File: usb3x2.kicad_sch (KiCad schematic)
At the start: 102 parts

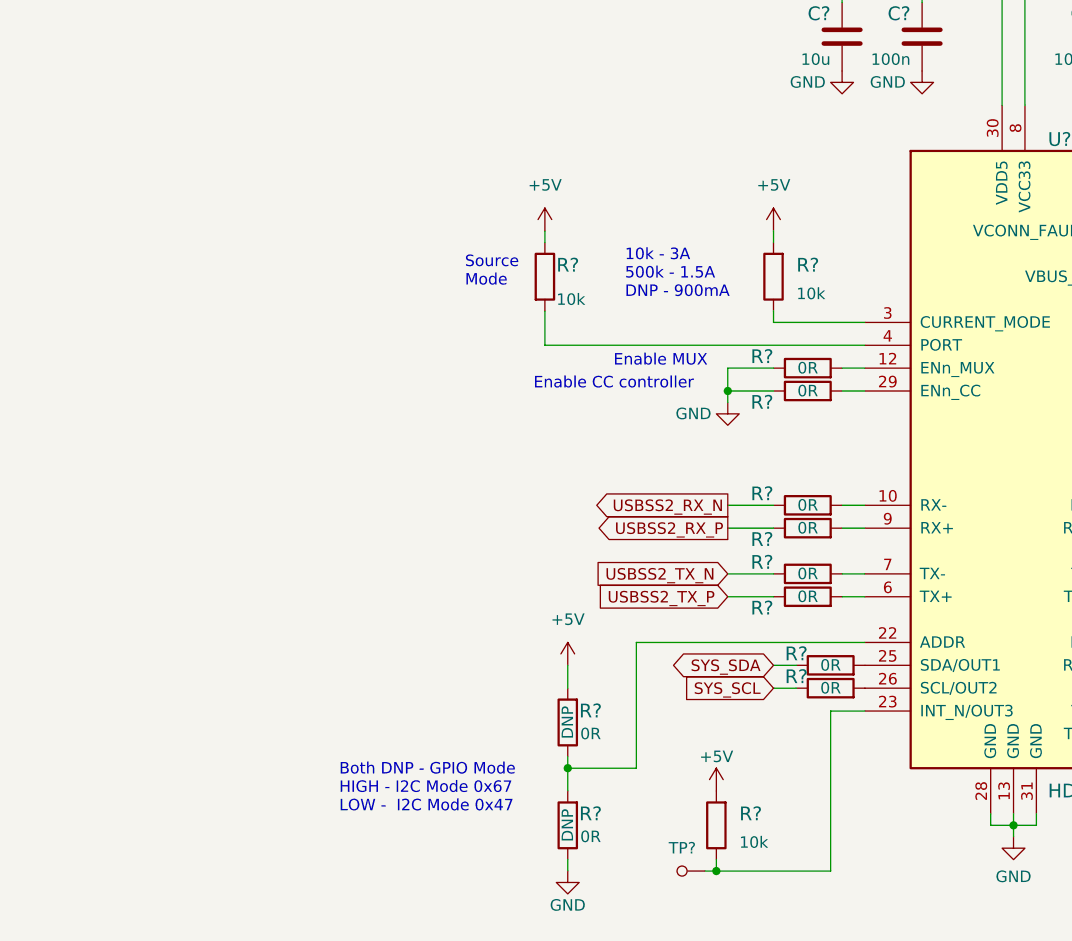
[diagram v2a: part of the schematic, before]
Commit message: Add labels to signals in usb3x2
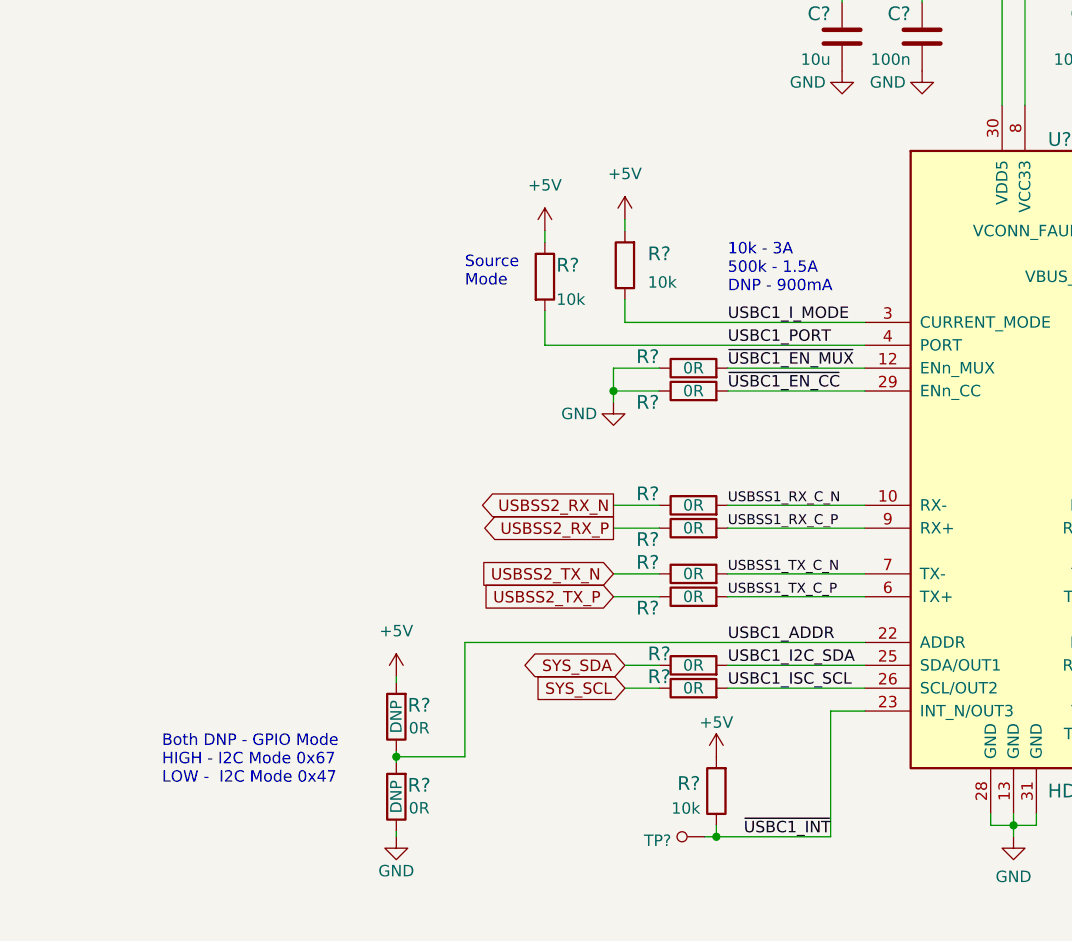
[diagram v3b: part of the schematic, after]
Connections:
- net USBC1_ADDR: now also R?.1, R?.2, U?.22 (ADDR)
- net USBC1_I2C_SDA: now also R?.2, U?.25 (SDA/OUT1)
- net USBC1_ISC_SCL: now also R?.2, U?.26 (SCL/OUT2)
- net USBC1_I_MODE: now also R?.1, U?.3 (CURRENT_MODE)
- net USBC1_PORT: now also R?.2, U?.4 (PORT)
- net USBSS1_RX_C_N: now also R?.2, U?.10 (RX-)
- net USBSS1_RX_C_P: now also R?.2, U?.9 (RX+)
- net USBSS1_TX_C_N: now also R?.2, U?.7 (TX-)
- net USBSS1_TX_C_P: now also R?.2, U?.6 (TX+)
- net ~{USBC1_EN_CC}: now also R?.2, U?.29 (ENn_CC)
- net ~{USBC1_EN_MUX}: now also R?.2, U?.12 (ENn_MUX)
- net ~{USBC1_INT}: now also R?.1, TP?.1, U?.23 (INT_N/OUT3)
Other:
- title: USB3 x2 -> Jetson Orin NX Baseboard
- moved on the sheet: R?, TP?

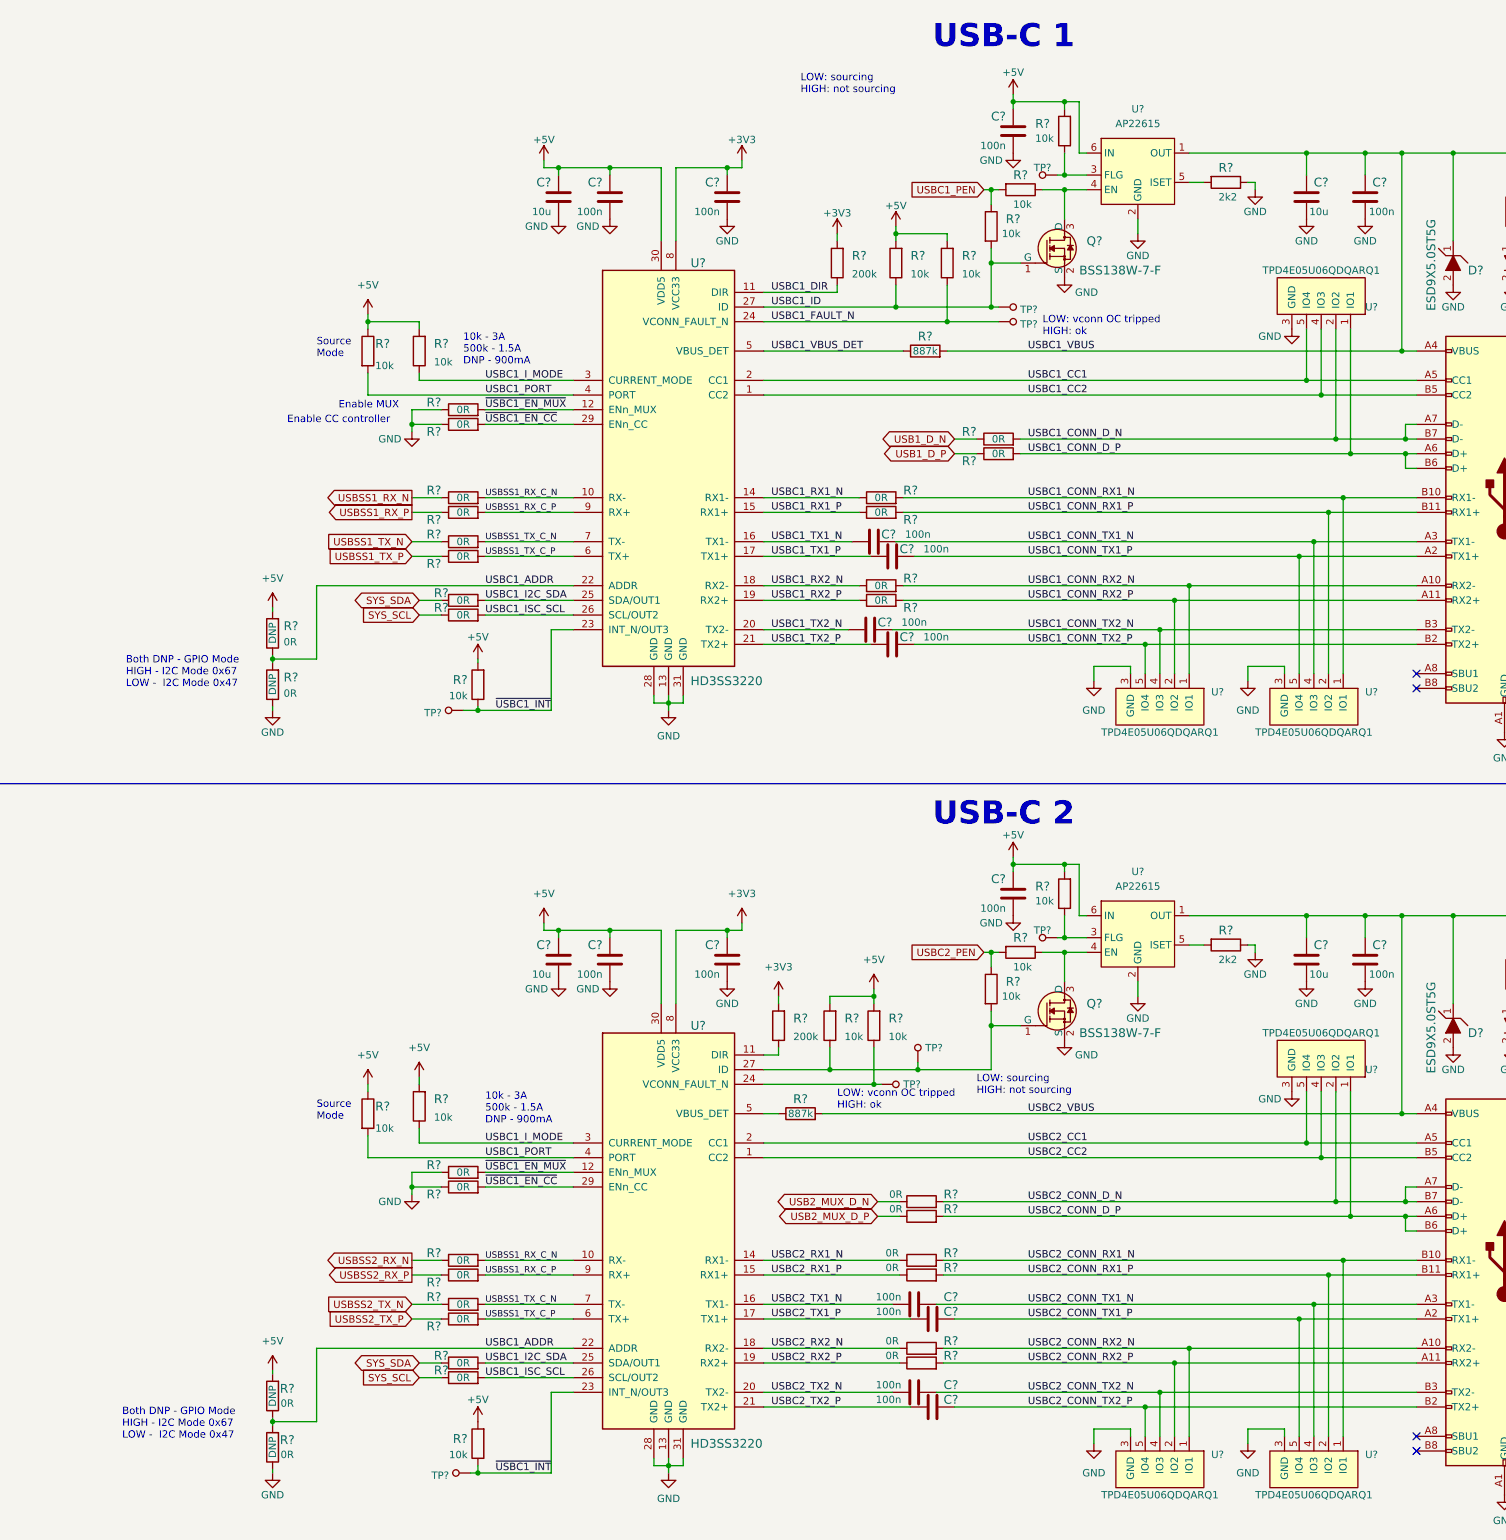
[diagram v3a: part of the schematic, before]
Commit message: Add labels to usb3x2
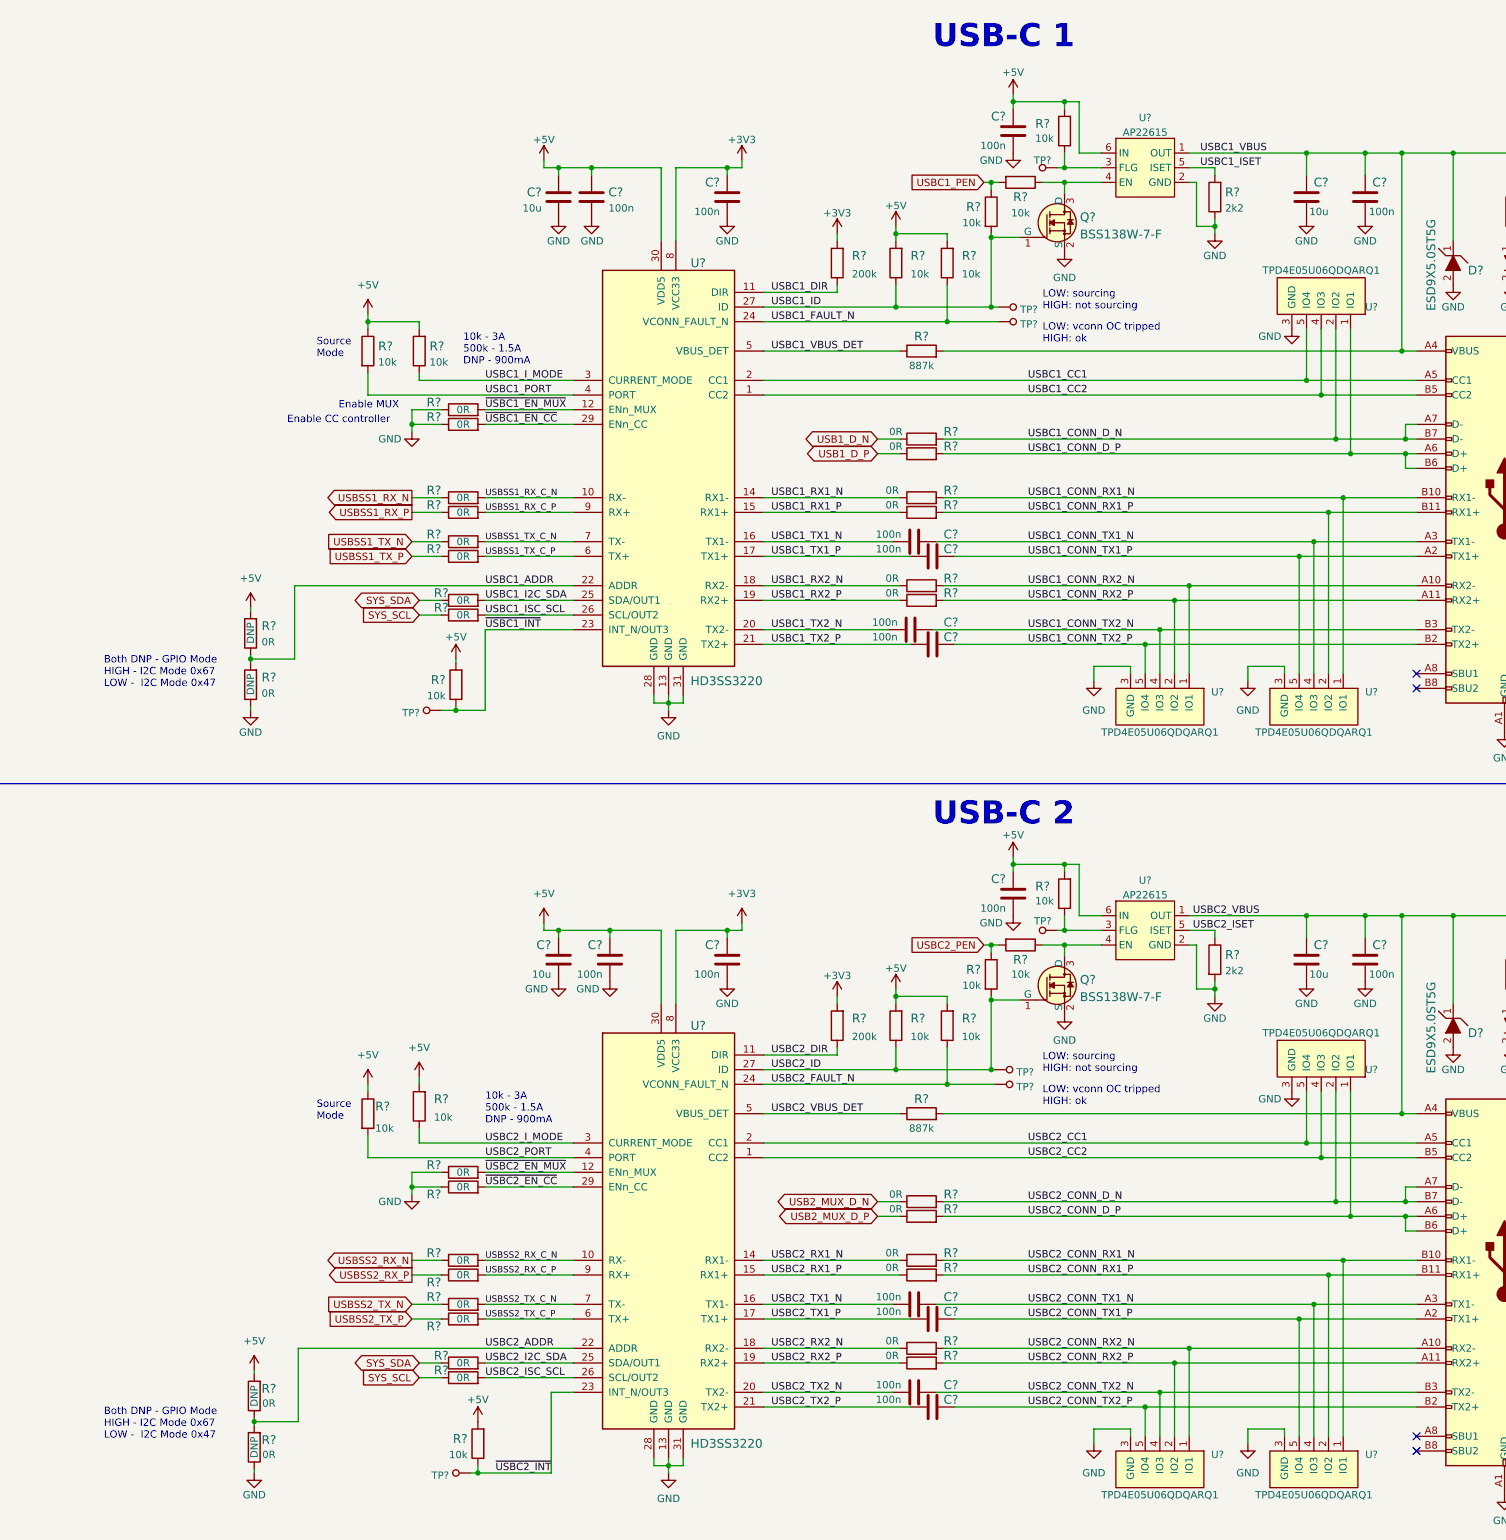
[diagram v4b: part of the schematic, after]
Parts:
- U?: MPN AP22615 -> AP22615AWU-7
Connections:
- net GND: now also R?.2; no longer R?.1
- net USBC1_ADDR: no longer R?.1, R?.2, U?.22 (ADDR)
- net USBC1_I2C_SDA: no longer R?.2, U?.25 (SDA/OUT1)
- net USBC1_ISC_SCL: no longer R?.2, U?.26 (SCL/OUT2)
- net USBC1_I_MODE: no longer R?.1, U?.3 (CURRENT_MODE)
- net USBC1_PORT: no longer R?.2, U?.4 (PORT)
- net USBSS1_RX_C_N: no longer R?.2, U?.10 (RX-)
- net USBSS1_RX_C_P: no longer R?.2, U?.9 (RX+)
- net USBSS1_TX_C_N: no longer R?.2, U?.7 (TX-)
- net USBSS1_TX_C_P: no longer R?.2, U?.6 (TX+)
- net ~{USBC1_EN_CC}: no longer R?.2, U?.29 (ENn_CC)
- net ~{USBC1_EN_MUX}: no longer R?.2, U?.12 (ENn_MUX)
- net ~{USBC1_INT}: no longer R?.1, TP?.1, U?.23 (INT_N/OUT3)
- net USBC1_ISET: now reaches R?.2, U?.5 (ISET)
- net USBC2_ISET: now reaches U?.5 (ISET)
- net USBC2_ISET: now also R?.1; no longer R?.2
- net USBC2_FAULT_N: now reaches R?.1, TP?.1, U?.24 (VCONN_FAULT_N)
- net USBC2_VBUS_DET: now reaches R?.1, U?.5 (VBUS_DET)
- net USBC2_ID: now reaches Q?.1 (G), R?.1, R?.2, TP?.1, U?.27 (ID)
- net USBC2_DIR: now reaches R?.1, U?.11 (DIR)
- new net USBC2_ADDR: R?.1, R?.2, U?.22 (ADDR)
- new net USBC2_I2C_SDA: R?.2, U?.25 (SDA/OUT1)
- new net USBC2_ISC_SCL: R?.2, U?.26 (SCL/OUT2)
- new net USBC2_I_MODE: R?.1, U?.3 (CURRENT_MODE)
- new net USBC2_PORT: R?.2, U?.4 (PORT)
- new net USBSS2_RX_C_N: R?.2, U?.10 (RX-)
- new net USBSS2_RX_C_P: R?.2, U?.9 (RX+)
- new net USBSS2_TX_C_N: R?.2, U?.7 (TX-)
- new net USBSS2_TX_C_P: R?.2, U?.6 (TX+)
- new net ~{USBC2_EN_CC}: R?.2, U?.29 (ENn_CC)
- new net ~{USBC2_EN_MUX}: R?.2, U?.12 (ENn_MUX)
- new net ~{USBC2_INT}: R?.1, TP?.1, U?.23 (INT_N/OUT3)
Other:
- moved on the sheet: C?, Q?, R?, TP?, U?

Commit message: Update AP22615 symbols
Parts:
- U?: MPN AP22615 -> AP22615AWU-7
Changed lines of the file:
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@@
     (pin "1")
   )
-  (symbol (lib_id "antmicroPMICPowerDistributionSwitchesLoadDrivers:AP22615") (at 226.06 41.91 0) (unit 1)
+  (symbol (lib_name "AP22615_1") (lib_id "antmicroPMICPowerDistributionSwitchesLoadDrivers:AP22615") (at 226.06 41.91 0) (unit 1)
     (in_bom yes) (on_board yes) (fields_autoplaced)
     (property "Reference" "U?" (id 0) (at 226.06 33.2572 0))
@@
       (effects (font (size 1.27 1.27)) hide)
     )
-    (property "MPN" "AP22615" (id 4) (at 226.06 63.5 0)
+    (property "MPN" "AP22615AWU-7 " (id 4) (at 226.06 63.5 0)
       (effects (font (size 1.27 1.27)) hide)
     )
